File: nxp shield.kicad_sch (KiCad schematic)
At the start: 6 parts, among them J1 Conn_02x10_Counter_Clockwise, J2 Conn_02x08_Top_Bottom, J3 Conn_02x08_Top_Bottom, J4 Conn_02x06_Top_Bottom, J5 Conn_01x08, J6 Conn_01x08

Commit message: fixed spacing
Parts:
- removed J1: Conn_02x10_Counter_Clockwise, Connector_PinHeader_2.54mm:PinHeader_2x10_P2.54mm_Vertical, symbol Connector_Generic:Conn_02x10_Counter_Clockwise
- removed J2, J3: Conn_02x08_Top_Bottom, Connector_PinHeader_2.54mm:PinHeader_2x08_P2.54mm_Vertical, symbol Connector_Generic:Conn_02x08_Top_Bottom
- removed J4: Conn_02x06_Top_Bottom, Connector_PinHeader_2.54mm:PinHeader_2x06_P2.54mm_Vertical, symbol Connector_Generic:Conn_02x06_Top_Bottom
- removed J5, J6: Conn_01x08, Connector_PinHeader_2.54mm:PinHeader_1x08_P2.54mm_Vertical, symbol Connector_Generic:Conn_01x08
- added U1: ~, frdm-mcxa153:FRDM-MCXA153, symbol frdm-mcxa153:frdm-mcxa153
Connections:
- new net GND: U1.30 (GND), U1.52 (GND), U1.54 (GND), U1.65 (GND), U1.66 (GND)

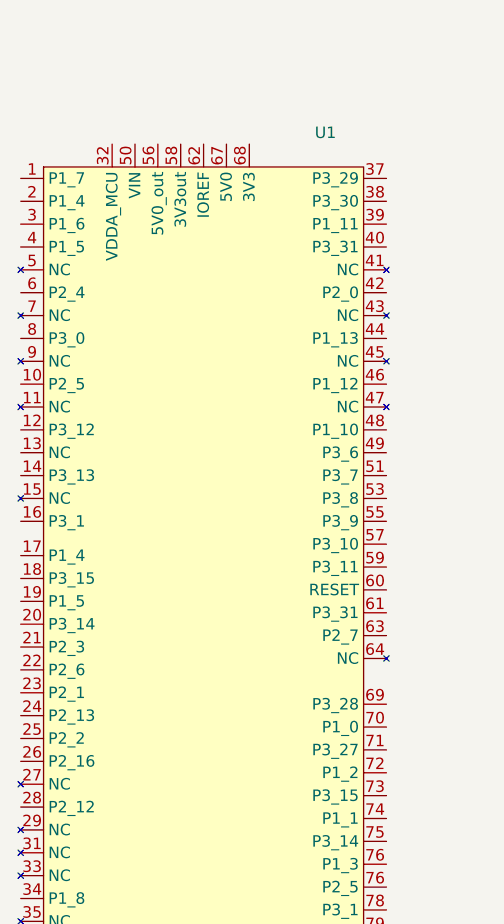
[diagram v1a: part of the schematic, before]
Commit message: fixed footprint, pin numbering and added ground plane
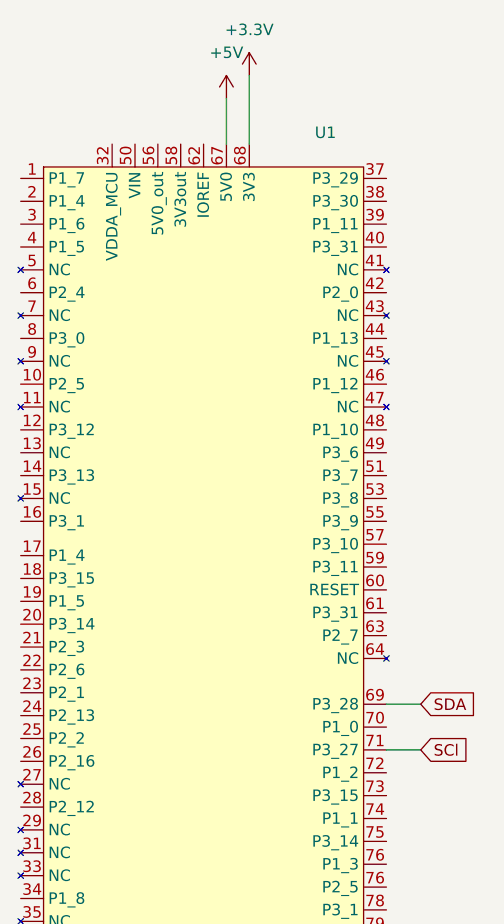
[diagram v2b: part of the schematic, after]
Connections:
- net +5V: now reaches U1.67 (5V0)
- net +3.3V: now reaches U1.68 (3V3)
- net SDA: now reaches U1.69 (P3_28)
- net SCl: now reaches U1.71 (P3_27)
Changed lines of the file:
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@@
+	(wire
+		(pts
+			(xy 102.87 59.69) (xy 102.87 67.31)
+		)
+		(stroke
+			(width 0)
+			(type default)
+		)
+	)
+	(wire
+		(pts
+			(xy 118.11 134.62) (xy 121.92 134.62)
+		)
+		(stroke
+			(width 0)
+			(type default)
+		)
+	)
 	(wire
 		(pts
@@
 	(wire
 		(pts
+			(xy 118.11 129.54) (xy 121.92 129.54)
+		)
+		(stroke
+			(width 0)
+			(type default)
+		)
+	)
+	(wire
+		(pts
+			(xy 100.33 62.23) (xy 100.33 67.31)
+		)
+		(stroke
+			(width 0)
+			(type default)
+		)
+	)
+	(wire
+		(pts
 			(xy 92.71 161.29) (xy 95.25 161.29)
 		)
@@
 			(width 0)
 			(type default)
+		)
+	)
+	(global_label "SCl"
+		(shape input)
+		(at 121.92 134.62 0)
+		(fields_autoplaced yes)
+		(effects
+			(font
+				(size 1.27 1.27)
+			)
+			(justify left)
+		)
+		(property "Intersheetrefs" "${INTERSHEET_REFS}"
+			(at 128.0499 134.62 0)
+			(effects
+				(font
+					(size 1.27 1.27)
+				)
+				(justify left)
+				(hide yes)
+			)
+		)
+	)
+	(global_label "SDA"
+		(shape input)
+		(at 121.92 129.54 0)
+		(fields_autoplaced yes)
+		(effects
+			(font
+				(size 1.27 1.27)
+			)
+			(justify left)
+		)
+		(property "Intersheetrefs" "${INTERSHEET_REFS}"
+			(at 128.4733 129.54 0)
+			(effects
+				(font
+					(size 1.27 1.27)
+				)
+				(justify left)
+				(hide yes)
+			)
 		)
 	)
@@
 					(unit 1)
 				)
+			)
+		)
+	)
+	(symbol
+		(lib_id "power:+3.3V")
+		(at 102.87 59.69 0)
+		(unit 1)
+		(exclude_from_sim no)
+		(in_bom yes)
+		(on_board yes)
+		(dnp no)
+		(fields_autoplaced yes)
+		(property "Reference" "#PWR03"
+			(at 102.87 63.5 0)
+			(effects
+				(font
+					(size 1.27 1.27)
+				)
+				(hide yes)
+			)
+		)
+		(property "Value" "+3.3V"
+			(at 102.87 54.61 0)
+			(effects
+				(font
+					(size 1.27 1.27)
+				)
+			)
+		)
+		(property "Footprint" ""
+			(at 102.87 59.69 0)
+			(effects
+				(font
+					(size 1.27 1.27)
+				)
+				(hide yes)
+			)
+		)
+		(property "Datasheet" ""
+			(at 102.87 59.69 0)
+			(effects
+				(font
+					(size 1.27 1.27)
+				)
+				(hide yes)
+			)
+		)
+		(property "Description" "Power symbol creates a global label with name \"+3.3V\""
+			(at 102.87 59.69 0)
+			(effects
+				(font
+					(size 1.27 1.27)
+				)
+				(hide yes)
+			)
+		)
+		(pin "1"
+		)
+		(instances
+			(project ""
+				(path "/3f6bc266-da46-45b3-b7d5-9083bf21ab21"
+					(reference "#PWR03")
+					(unit 1)
+				)
+			)
+		)
+	)
+	(symbol
+		(lib_id "power:+5V")
+		(at 100.33 62.23 0)
+		(unit 1)
+		(exclude_from_sim no)
+		(in_bom yes)
+		(on_board yes)
+		(dnp no)
+		(fields_autoplaced yes)
+		(property "Reference" "#PWR02"
+			(at 100.33 66.04 0)
+			(effects
+				(font
+					(size 1.27 1.27)
+				)
+				(hide yes)
+			)
+		)
+		(property "Value" "+5V"
+			(at 100.33 57.15 0)
+			(effects
+				(font
+					(size 1.27 1.27)
+				)
+			)
+		)
+		(property "Footprint" ""
+			(at 100.33 62.23 0)
+			(effects
+				(font
+					(size 1.27 1.27)
+				)
+				(hide yes)
+			)
+		)
+		(property "Datasheet" ""
+			(at 100.33 62.23 0)
+			(effects
+				(font
+					(size 1.27 1.27)
+				)
+				(hide yes)
+			)
+		)
+		(property "Description" "Power symbol creates a global label with name \"+5V\""
+			(at 100.33 62.23 0)
+			(effects
+				(font
+					(size 1.27 1.27)
+				)
+				(hide yes)
+			)
+		)
+		(pin "1"
+		)
+		(instances
+			(project ""
+				(path "/3f6bc266-da46-45b3-b7d5-9083bf21ab21"
+					(reference "#PWR02")
+					(unit 1)
+				)
